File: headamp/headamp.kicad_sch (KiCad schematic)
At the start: 91 parts, among them J1 MAINS 230V, J401 IN L (RCA), J402 IN R (RCA), J403 jack 6,3mm TRS (DT 770 M 80R), K1 9V, SW1 ON/OFF, SW2 S2 wokal, SW202 S2 wokal (P), SW401 S1 crossfeed, T1 OPT SE 5k:80R (>=25H, 45mA), T201 OPT SE 5k:80R (>=25H, 45mA), T301 EI84 100VA: 230V : 250V/0,15A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, U1 ECC82, U2 EL84 (trioda), U202 EL84 (trioda), U301 LD1085 (LDO)

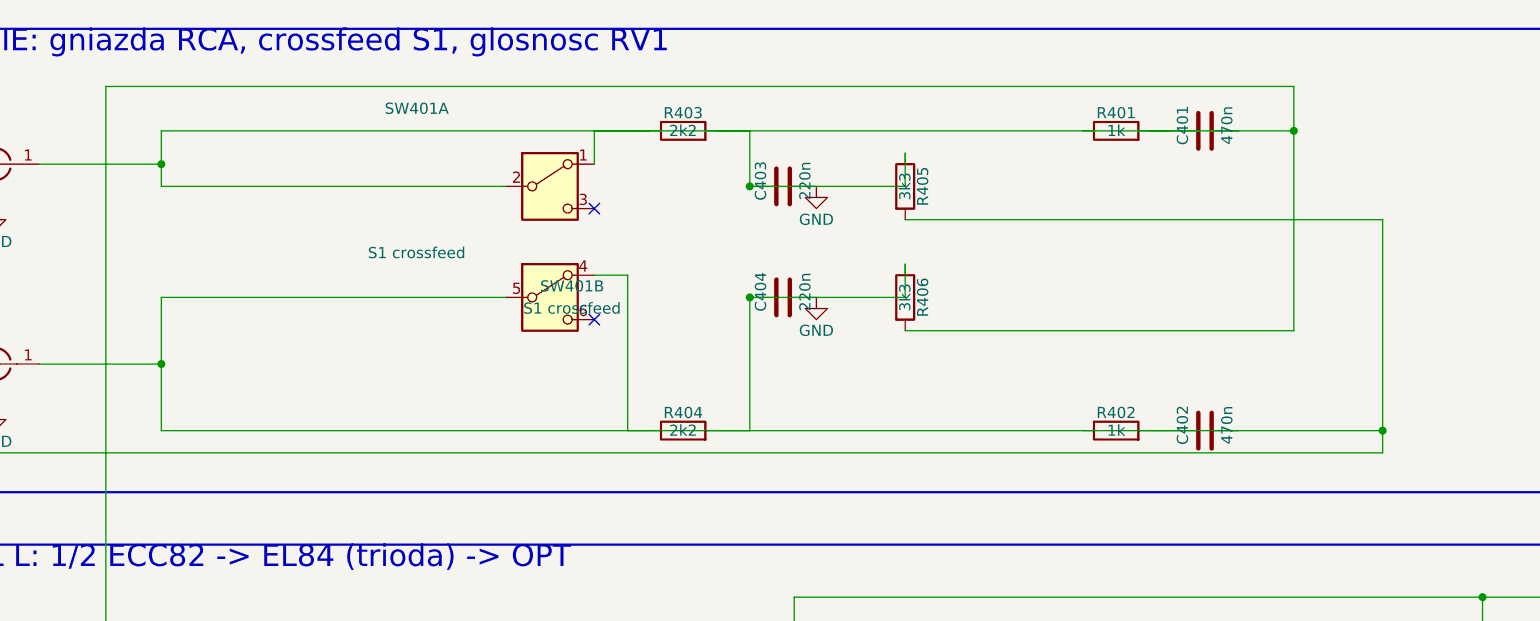
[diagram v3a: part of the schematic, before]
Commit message: headamp: crossfeed S1 przelacza galaz krzyzowa po stronie wyjscia (czysty tor prosty przy OFF) + sim
Poprzednia topologia (S1 na wejsciu galezi krzyzowej) zostawiala R405/R406+
C403/C404 jako obciazenie wyjsc toru prostego nawet przy S1 OFF - ugiecie
basu ~1,4 dB (symulacja porownawcza w sim/crossfeed_sw.cir, wariant "OFF
stara topologia"). Po przeniesieniu SW401 na wyjscie galezi krzyzowej (za
R405/R406, przed wspolnym wezlem z torem prostym), pozycja OFF odcina cala
galaz od wyjsc - odchylka od plaskiej ~0,17 dB (tylko C401/C402 w torze
prostym). check.py zaktualizowany pod nowa topologie (58 asercji OK), ERC
0 bledow/0 ostrzezen, regeneracja idempotentna (dwa uruchomienia gen.py
daja identyczny plik, zweryfikowane md5).

Co-Authored-By: Claude Sonnet 5 <noreply@anthropic.com>
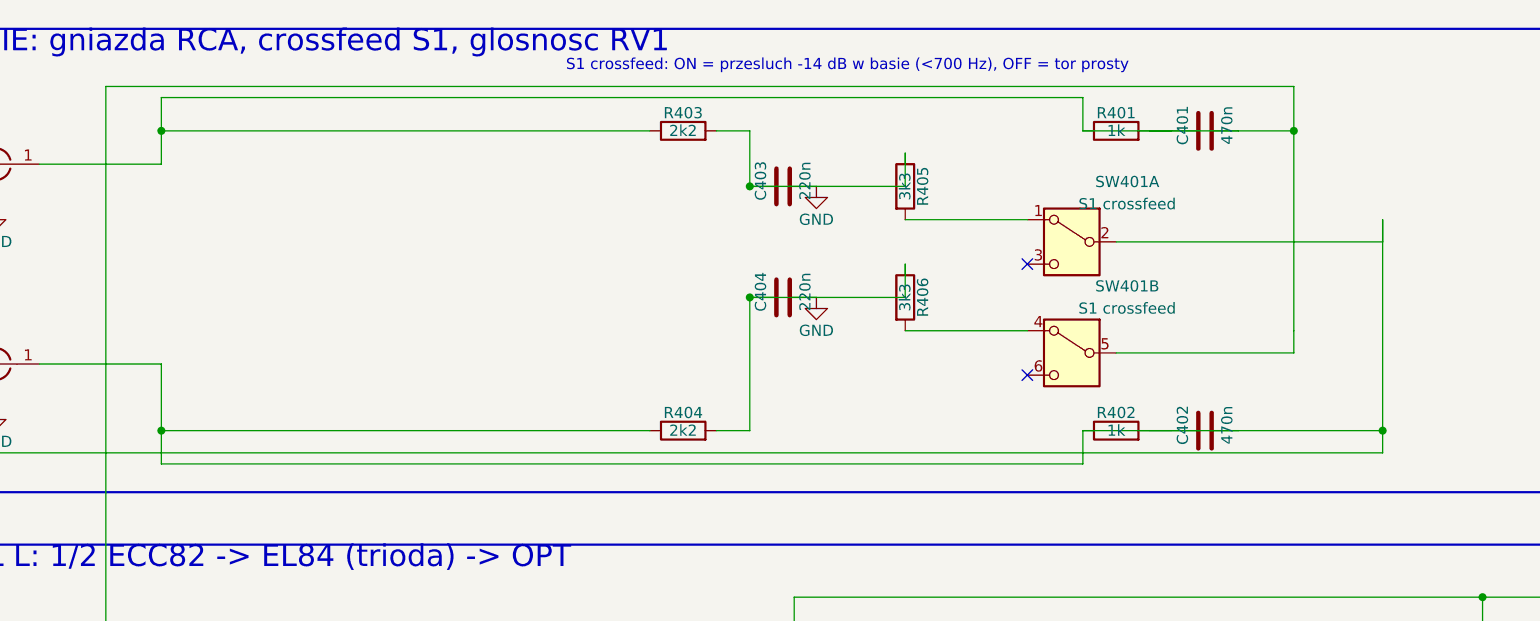
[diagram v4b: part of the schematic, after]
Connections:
- net at C402.1, C402.2, J402.1 (In)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: now also SW401.2 (B); no longer C404.1, R404.2, R405.2, R406.1, SW401.4 (A), SW401.5 (B)
- net at C401.1, C401.2, J401.1 (In)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: now also SW401.5 (B); no longer C403.1, R403.2, R405.1, R406.2, SW401.1 (A), SW401.2 (B)
- new net: C404.1, R404.2, R406.1
- new net: R406.2, SW401.4 (A)
- new net: C403.1, R403.2, R405.1
- new net: R405.2, SW401.1 (A)
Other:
- note added: "S1 crossfeed: ON = przesluch -14 dB w basie (<700 Hz), OFF = tor prosty"
- moved on the sheet: SW401A, SW401B
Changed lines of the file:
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@@
   (junction (at 185.42 218.44) (diameter 0))
   (junction (at 196.85 185.42) (diameter 0))
-  (junction (at 45.72 30.48) (diameter 0))
-  (junction (at 45.72 53.34) (diameter 0))
+  (junction (at 45.72 26.67) (diameter 0))
+  (junction (at 45.72 60.96) (diameter 0))
   (junction (at 175.26 26.67) (diameter 0))
   (junction (at 185.42 60.96) (diameter 0))
@@
   (wire (pts (xy 31.75 30.48) (xy 45.72 30.48)) (stroke (width 0) (type default)))
   (wire (pts (xy 45.72 30.48) (xy 45.72 26.67)) (stroke (width 0) (type default)))
-  (wire (pts (xy 45.72 26.67) (xy 151.13 26.67)) (stroke (width 0) (type default)))
-  (wire (pts (xy 45.72 30.48) (xy 45.72 33.02)) (stroke (width 0) (type default)))
-  (wire (pts (xy 45.72 33.02) (xy 85.09 33.02)) (stroke (width 0) (type default)))
+  (wire (pts (xy 45.72 26.67) (xy 101.6 26.67)) (stroke (width 0) (type default)))
+  (wire (pts (xy 45.72 26.67) (xy 45.72 22.86)) (stroke (width 0) (type default)))
+  (wire (pts (xy 45.72 22.86) (xy 151.13 22.86)) (stroke (width 0) (type default)))
+  (wire (pts (xy 151.13 22.86) (xy 151.13 26.67)) (stroke (width 0) (type default)))
   (wire (pts (xy 31.75 53.34) (xy 45.72 53.34)) (stroke (width 0) (type default)))
   (wire (pts (xy 45.72 53.34) (xy 45.72 60.96)) (stroke (width 0) (type default)))
-  (wire (pts (xy 45.72 60.96) (xy 151.13 60.96)) (stroke (width 0) (type default)))
-  (wire (pts (xy 45.72 53.34) (xy 45.72 45.72)) (stroke (width 0) (type default)))
-  (wire (pts (xy 45.72 45.72) (xy 85.09 45.72)) (stroke (width 0) (type default)))
-  (wire (pts (xy 95.25 30.48) (xy 95.25 26.67)) (stroke (width 0) (type default)))
-  (wire (pts (xy 95.25 26.67) (xy 101.6 26.67)) (stroke (width 0) (type default)))
-  (wire (pts (xy 95.25 43.18) (xy 99.06 43.18)) (stroke (width 0) (type default)))
-  (wire (pts (xy 99.06 43.18) (xy 99.06 60.96)) (stroke (width 0) (type default)))
-  (wire (pts (xy 99.06 60.96) (xy 101.6 60.96)) (stroke (width 0) (type default)))
+  (wire (pts (xy 45.72 60.96) (xy 101.6 60.96)) (stroke (width 0) (type default)))
+  (wire (pts (xy 45.72 60.96) (xy 45.72 64.77)) (stroke (width 0) (type default)))
+  (wire (pts (xy 45.72 64.77) (xy 151.13 64.77)) (stroke (width 0) (type default)))
+  (wire (pts (xy 151.13 64.77) (xy 151.13 60.96)) (stroke (width 0) (type default)))
   (wire (pts (xy 151.13 26.67) (xy 161.29 26.67)) (stroke (width 0) (type default)))
   (wire (pts (xy 158.75 26.67) (xy 168.91 26.67)) (stroke (width 0) (type default)))
@@
   (wire (pts (xy 113.03 33.02) (xy 130.81 33.02)) (stroke (width 0) (type default)))
   (wire (pts (xy 130.81 33.02) (xy 130.81 29.21)) (stroke (width 0) (type default)))
-  (wire (pts (xy 130.81 36.83) (xy 185.42 36.83)) (stroke (width 0) (type default)))
+  (wire (pts (xy 130.81 36.83) (xy 144.78 36.83)) (stroke (width 0) (type default)))
+  (wire (pts (xy 154.94 39.37) (xy 185.42 39.37)) (stroke (width 0) (type default)))
+  (wire (pts (xy 185.42 39.37) (xy 185.42 36.83)) (stroke (width 0) (type default)))
   (wire (pts (xy 109.22 60.96) (xy 113.03 60.96)) (stroke (width 0) (type default)))
   (wire (pts (xy 113.03 60.96) (xy 113.03 45.72)) (stroke (width 0) (type default)))
   (wire (pts (xy 113.03 45.72) (xy 130.81 45.72)) (stroke (width 0) (type default)))
   (wire (pts (xy 130.81 45.72) (xy 130.81 41.91)) (stroke (width 0) (type default)))
-  (wire (pts (xy 130.81 49.53) (xy 175.26 49.53)) (stroke (width 0) (type default)))
+  (wire (pts (xy 130.81 49.53) (xy 144.78 49.53)) (stroke (width 0) (type default)))
+  (wire (pts (xy 154.94 52.07) (xy 175.26 52.07)) (stroke (width 0) (type default)))
+  (wire (pts (xy 175.26 52.07) (xy 175.26 49.53)) (stroke (width 0) (type default)))
   (wire (pts (xy 222.25 102.87) (xy 285.75 102.87)) (stroke (width 0) (type default)))
   (wire (pts (xy 285.75 102.87) (xy 285.75 193.04)) (stroke (width 0) (type default)))
@@
   (wire (pts (xy 55.88 355.6) (xy 66.04 355.6)) (stroke (width 0) (type default)))
   (wire (pts (xy 66.04 355.6) (xy 76.2 355.6)) (stroke (width 0) (type default)))
-  (no_connect (at 95.25 35.56))
-  (no_connect (at 95.25 48.26))
+  (no_connect (at 144.78 41.91))
+  (no_connect (at 144.78 54.61))
   (no_connect (at 250.19 299.72))
   (rectangle (start 15 15) (end 255 68) (stroke (width 0.254) (type default)) (fill (type none)))
@@
   (label "V_RAW" (at 320.04 339.09 0) (effects (font (size 1.27 1.27)) (justify left bottom)))
   (label "ELEV" (at 281.94 361.95 0) (effects (font (size 1.27 1.27)) (justify right bottom)))
+  (text "S1 crossfeed: ON = przesluch -14 dB w basie (<700 Hz), OFF = tor prosty" (at 92 20 0) (effects (font (size 1.27 1.27)) (justify left bottom)))
   (text "PE -> wlasna sruba M4 na chassis" (at 22.86 340.36 0) (effects (font (size 1.27 1.27)) (justify left bottom)))
   (text "230V/0,15A (HT)" (at 88.9 312.42 0) (effects (font (size 1.27 1.27)) (justify left bottom)))
@@
     (instances (project "headamp" (path "/fd162765-1b28-469c-8099-083c76e823f0" (reference "J402") (unit 1))))
   )
-  (symbol (lib_id "Switch:SW_DPDT_x2") (at 90.17 33.02 0) (unit 1)
-    (in_bom yes) (on_board yes) (dnp no)
-    (property "Reference" "SW401" (at 74.93 24.13 0) (effects (font (size 1.27 1.27))))
-    (property "Value" "S1 crossfeed" (at 74.93 40.64 0) (effects (font (size 1.27 1.27))))
-    (property "Footprint" "" (at 90.17 33.02 0) (effects (font (size 1.27 1.27)) hide))
-    (property "Datasheet" "" (at 90.17 33.02 0) (effects (font (size 1.27 1.27)) hide))
+  (symbol (lib_id "Switch:SW_DPDT_x2") (at 149.86 39.37 0) (mirror y) (unit 1)
+    (in_bom yes) (on_board yes) (dnp no)
+    (property "Reference" "SW401" (at 156.21 32.51 0) (effects (font (size 1.27 1.27))))
+    (property "Value" "S1 crossfeed" (at 156.21 35.05 0) (effects (font (size 1.27 1.27))))
+    (property "Footprint" "" (at 149.86 39.37 0) (effects (font (size 1.27 1.27)) hide))
+    (property "Datasheet" "" (at 149.86 39.37 0) (effects (font (size 1.27 1.27)) hide))
     (pin "1")
     (pin "2")
@@
     (instances (project "headamp" (path "/fd162765-1b28-469c-8099-083c76e823f0" (reference "SW401") (unit 1))))
   )
-  (symbol (lib_id "Switch:SW_DPDT_x2") (at 90.17 45.72 0) (unit 2)
-    (in_bom yes) (on_board yes) (dnp no)
-    (property "Reference" "SW401" (at 92.71 44.45 0) (effects (font (size 1.27 1.27))))
-    (property "Value" "S1 crossfeed" (at 92.71 46.99 0) (effects (font (size 1.27 1.27))))
-    (property "Footprint" "" (at 90.17 45.72 0) (effects (font (size 1.27 1.27)) hide))
-    (property "Datasheet" "" (at 90.17 45.72 0) (effects (font (size 1.27 1.27)) hide))
+  (symbol (lib_id "Switch:SW_DPDT_x2") (at 149.86 52.07 0) (mirror y) (unit 2)
+    (in_bom yes) (on_board yes) (dnp no)
+    (property "Reference" "SW401" (at 156.21 44.45 0) (effects (font (size 1.27 1.27))))
+    (property "Value" "S1 crossfeed" (at 156.21 46.99 0) (effects (font (size 1.27 1.27))))
+    (property "Footprint" "" (at 149.86 52.07 0) (effects (font (size 1.27 1.27)) hide))
+    (property "Datasheet" "" (at 149.86 52.07 0) (effects (font (size 1.27 1.27)) hide))
     (pin "4")
     (pin "5")
